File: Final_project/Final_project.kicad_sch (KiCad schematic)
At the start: 33 parts, among them U1 RP2040, U2 MCP1702T-3302E_CB, U3 ESP32-WROOM-32

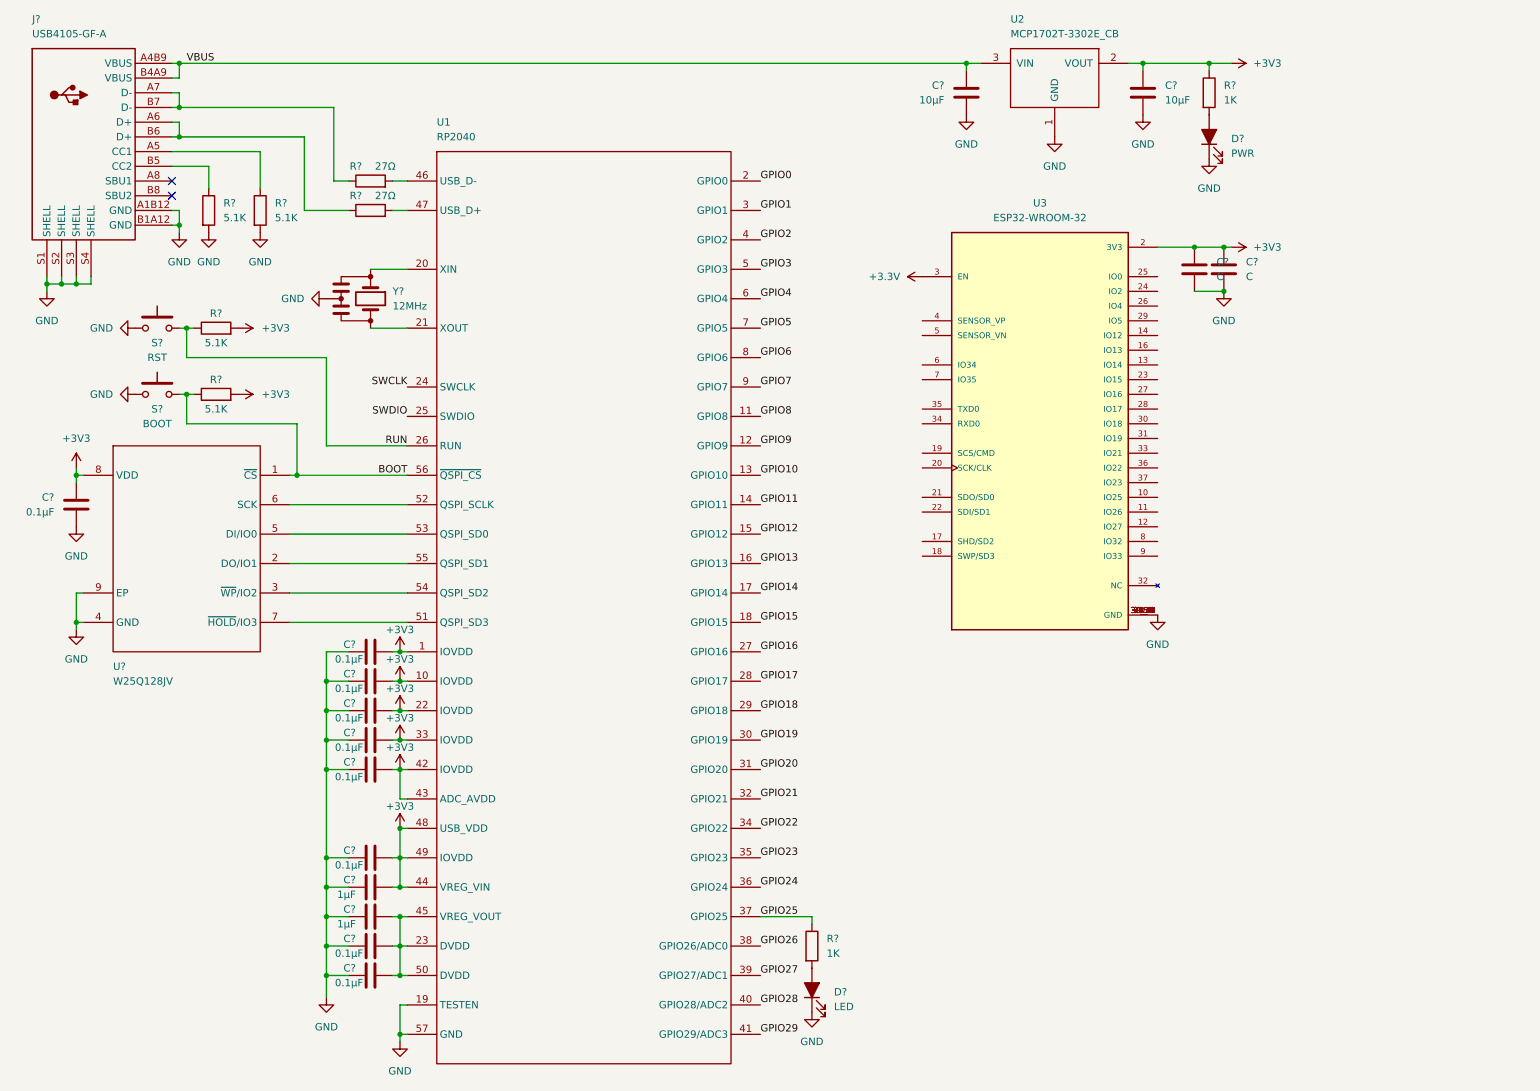
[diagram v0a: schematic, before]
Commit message: Add library and hierarchical schematic
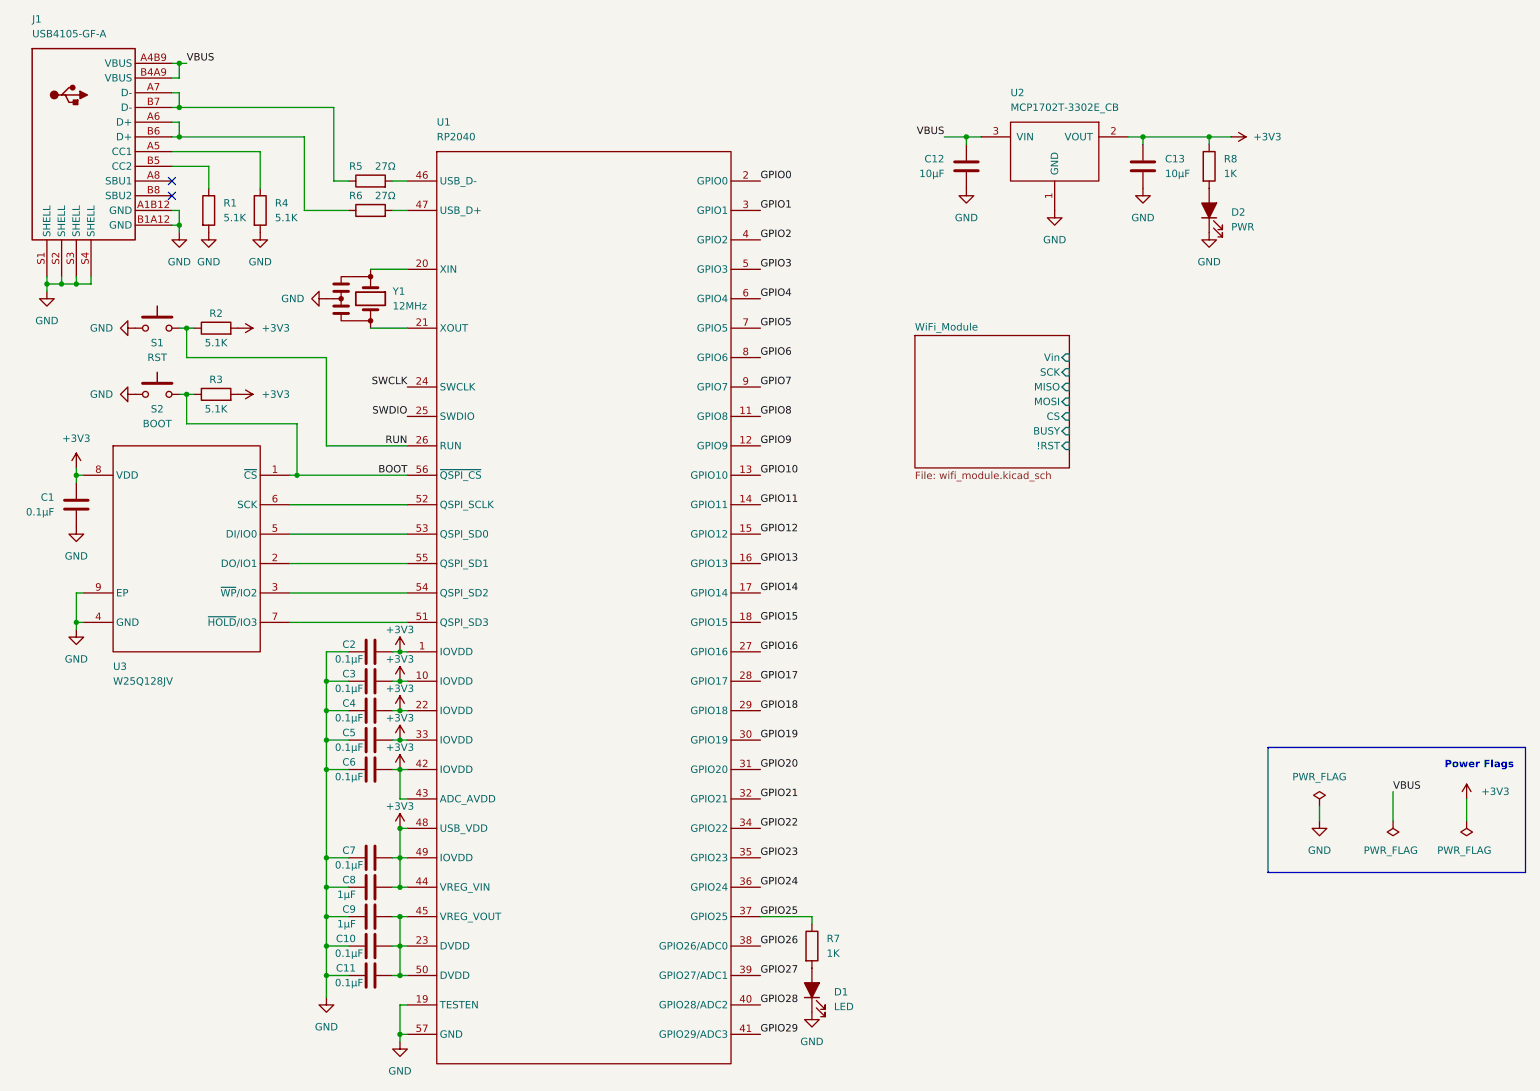
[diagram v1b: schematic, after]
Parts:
- removed C? (x2): C, symbol Device:C
- removed U3: ESP32-WROOM-32, MODULE_ESP32-WROOM-32, symbol ESP32-WROOM-32:ESP32-WROOM-32
- C1, C10, C11, C2, C3, C4, C5, C6, C7: renamed from C?; footprint Eclectronics_mp3:CL10B104JB8NNNC -> Final_project:CL10B104JB8NNNC
- C12, C13: renamed from C?; footprint Eclectronics_mp3:GRM188R61E106KA73D -> Final_project:GRM188R61E106KA73D
- C8, C9: renamed from C?; footprint Eclectronics_mp3:CL10B105KA8NNNC -> Final_project:CL10B105KA8NNNC
- D1: renamed from D?; footprint Eclectronics_mp3:LTST-C170TBKT -> Final_project:LTST-C170TBKT
- D2: renamed from D?; footprint Eclectronics_mp3:LTST-C170TGKT -> Final_project:LTST-C170TGKT
- J1: renamed from J?; footprint Eclectronics_mp3:USB4105-GF-A -> Final_project:USB4105-GF-A
- R1, R2, R3, R4: renamed from R?; footprint Eclectronics_mp3:RES_ERJ3EKF5101V -> Final_project:RES_ERJ3EKF5101V
- R5, R6, R7, R8: renamed from R?; footprint Eclectronics_mp3:RC0603FR-071KL -> Final_project:RC0603FR-071KL
- S1, S2: renamed from S?; footprint Eclectronics_mp3:KXT321LHS -> Final_project:KXT321LHS
- U1: footprint Eclectronics_mp3:RP2040 -> Final_project:RP2040
- U3: renamed from U?; footprint Eclectronics_mp3:MIC_WSON-8-M -> Final_project:MIC_WSON-8-M
- Y1: renamed from Y?; footprint Eclectronics_mp3:CSTNE -> Final_project:CSTNE
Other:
- added sheet WiFi_Module (wifi_module.kicad_sch)
- note added: "Power Flags"
- moved on the sheet: C12, C13, D2, R8, U2

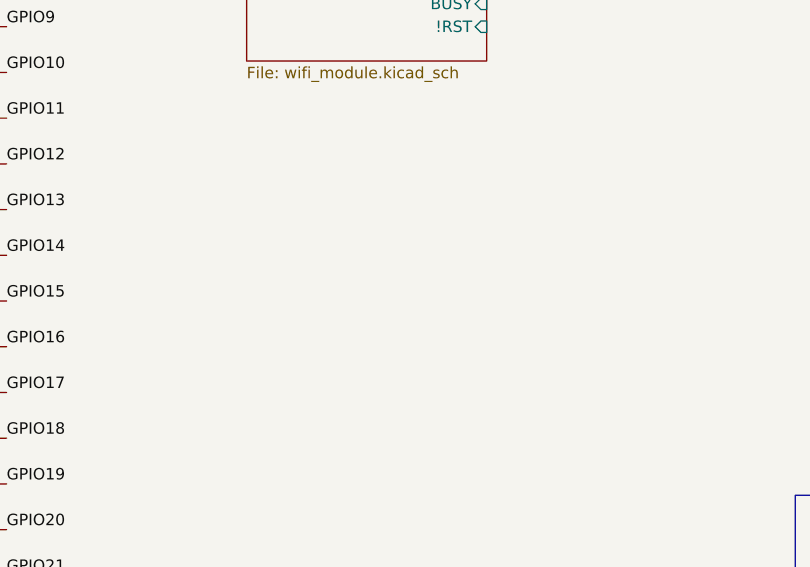
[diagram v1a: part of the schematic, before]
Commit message: added audiojack
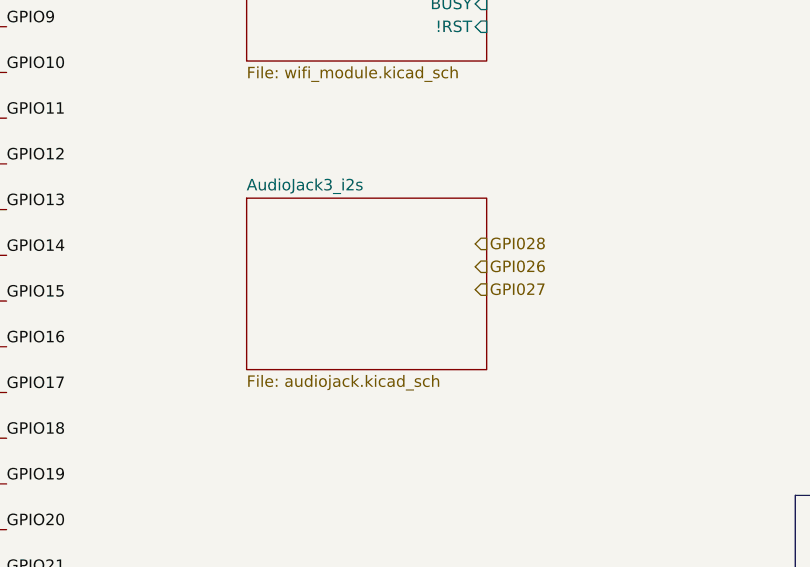
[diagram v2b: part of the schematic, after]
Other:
- added sheet AudioJack3_i2s (audiojack.kicad_sch)
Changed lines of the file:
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@@
     (effects (font (size 1.27 1.27)) (justify left bottom))
+  )
+  (hierarchical_label "GPI026" (shape input) (at 199.39 114.3 0)
+    (effects (font (size 1.27 1.27)) (justify left))
+  )
+  (hierarchical_label "GPI028" (shape input) (at 199.39 111.76 0)
+    (effects (font (size 1.27 1.27)) (justify left))
+  )
+  (hierarchical_label "GPI027" (shape input) (at 199.39 116.84 0)
+    (effects (font (size 1.27 1.27)) (justify left))
   )
   (symbol (lib_id "Device:C") (at 80.01 138.43 270) (unit 1)
@@
     )
   )
+  (sheet (at 173.99 106.68) (size 26.67 19.05) (fields_autoplaced)
+    (stroke (width 0.1524) (type solid) (color 0 0 0 0))
+    (fill (color 255 255 194 1.0000))
+    (property "Sheet name" "AudioJack3_i2s" (id 0) (at 173.99 105.9684 0)
+      (effects (font (size 1.27 1.27)) (justify left bottom))
+    )
+    (property "Sheet file" "audiojack.kicad_sch" (id 1) (at 173.99 126.3146 0)
+      (effects (font (size 1.27 1.27)) (justify left top))
+    )
+  )
   (sheet_instances
     (path "/" (page "1"))
     (path "/5f380518-a4aa-4cf5-aa47-79ba18474bc7" (page "2"))
+    (path "/a587f9f9-6d27-4989-a344-d47a4b55e4be" (page "3"))
   )
   (symbol_instances
@@
       (reference "#PWR0132") (unit 1) (value "GND") (footprint "")
     )
+    (path "/a587f9f9-6d27-4989-a344-d47a4b55e4be/0758e25a-39ba-4d34-abca-2bb40d5af830"
+      (reference "#PWR?") (unit 1) (value "GND") (footprint "")
+    )
+    (path "/a587f9f9-6d27-4989-a344-d47a4b55e4be/1b14fa98-daa4-474f-ab59-8b8ff9ad2252"
+      (reference "#PWR?") (unit 1) (value "GND") (footprint "")
+    )
+    (path "/a587f9f9-6d27-4989-a344-d47a4b55e4be/4261c671-797a-4dce-b779-2a1cca3a497a"
+      (reference "#PWR?") (unit 1) (value "GND") (footprint "")
+    )
+    (path "/a587f9f9-6d27-4989-a344-d47a4b55e4be/49961937-da64-4a79-b32e-b550e5b13812"
+      (reference "#PWR?") (unit 1) (value "GND") (footprint "")
+    )
+    (path "/a587f9f9-6d27-4989-a344-d47a4b55e4be/4a0c82ab-f8f8-4889-9bab-585f3ddf17f0"
+      (reference "#PWR?") (unit 1) (value "GND") (footprint "")
+    )
+    (path "/a587f9f9-6d27-4989-a344-d47a4b55e4be/60d3bdc0-5ca1-4a26-b977-3b85a79f9bd8"
+      (reference "#PWR?") (unit 1) (value "GND") (footprint "")
+    )
+    (path "/a587f9f9-6d27-4989-a344-d47a4b55e4be/6768cd5a-a081-418d-bb8c-15ae6a2958b1"
+      (reference "#PWR?") (unit 1) (value "GND") (footprint "")
+    )
+    (path "/a587f9f9-6d27-4989-a344-d47a4b55e4be/6a4163df-9085-4be2-840b-f3d0d2548868"
+      (reference "#PWR?") (unit 1) (value "+3.3V") (footprint "")
+    )
+    (path "/a587f9f9-6d27-4989-a344-d47a4b55e4be/74c14a05-ea6b-4019-8abd-25eb1a6fc3bc"
+      (reference "#PWR?") (unit 1) (value "GND") (footprint "")
+    )
+    (path "/a587f9f9-6d27-4989-a344-d47a4b55e4be/8d23dbde-8b01-4c96-b6b9-2cd0d701c902"
+      (reference "#PWR?") (unit 1) (value "+3.3VA") (footprint "")
+    )
+    (path "/a587f9f9-6d27-4989-a344-d47a4b55e4be/941fd3b4-a86c-4982-94f3-d22033298fcf"
+      (reference "#PWR?") (unit 1) (value "GND") (footprint "")
+    )
+    (path "/a587f9f9-6d27-4989-a344-d47a4b55e4be/d754a0cf-27fb-43d7-96e5-e22e0806c88b"
+      (reference "#PWR?") (unit 1) (value "+3.3V") (footprint "")
+    )
+    (path "/a587f9f9-6d27-4989-a344-d47a4b55e4be/fdd1049d-4353-4894-a8db-3df85b208654"
+      (reference "#PWR?") (unit 1) (value "GND") (footprint "")
+    )
     (path "/4185e825-d3db-49f7-84c3-1d674f768766"
       (reference "C1") (unit 1) (value "0.1µF") (footprint "Final_project:CL10B104JB8NNNC")
@@
       (reference "C15") (unit 1) (value "C") (footprint "Capacitor_SMD:C_0603_1608Metric")
     )
+    (path "/a587f9f9-6d27-4989-a344-d47a4b55e4be/108086f3-c1df-4566-84bd-fbc60614202b"
+      (reference "C?") (unit 1) (value "10u") (footprint "Capacitor_SMD:C_0603_1608Metric")
+    )
+    (path "/a587f9f9-6d27-4989-a344-d47a4b55e4be/32442a1c-8e05-4bad-b894-204e8dac19bb"
+      (reference "C?") (unit 1) (value "2.2n") (footprint "Capacitor_SMD:C_0402_1005Metric")
+    )
+    (path "/a587f9f9-6d27-4989-a344-d47a4b55e4be/4c6a2e57-abe7-478c-a1a6-024cf77305b0"
+      (reference "C?") (unit 1) (value "100n") (footprint "Capacitor_SMD:C_0402_1005Metric")
+    )
+    (path "/a587f9f9-6d27-4989-a344-d47a4b55e4be/6ca33c87-f79e-4a26-9f94-3927f1b5c179"
+      (reference "C?") (unit 1) (value "2.2u") (footprint "Capacitor_SMD:C_0603_1608Metric")
+    )
+    (path "/a587f9f9-6d27-4989-a344-d47a4b55e4be/70985074-b4dd-4282-bf81-f45bdab6ee8e"
+      (reference "C?") (unit 1) (value "10u") (footprint "Capacitor_SMD:C_0603_1608Metric")
+    )
+    (path "/a587f9f9-6d27-4989-a344-d47a4b55e4be/825af33a-d88e-4844-a2b2-fcc455893256"
+      (reference "C?") (unit 1) (value "100n") (footprint "Capacitor_SMD:C_0402_1005Metric")
+    )
+    (path "/a587f9f9-6d27-4989-a344-d47a4b55e4be/a8ef7a4d-08e8-40a1-96aa-2409cbe8b2f4"
+      (reference "C?") (unit 1) (value "2.2u") (footprint "Capacitor_SMD:C_0603_1608Metric")
+    )
+    (path "/a587f9f9-6d27-4989-a344-d47a4b55e4be/b2ae8a85-0718-4b79-bbda-e04acbe0ead8"
+      (reference "C?") (unit 1) (value "100n") (footprint "Capacitor_SMD:C_0402_1005Metric")
+    )
+    (path "/a587f9f9-6d27-4989-a344-d47a4b55e4be/b6bd64e6-b71d-475f-8470-2eb9494b5085"
+      (reference "C?") (unit 1) (value "2.2n") (footprint "Capacitor_SMD:C_0402_1005Metric")
+    )
+    (path "/a587f9f9-6d27-4989-a344-d47a4b55e4be/e7da94f5-848e-40b4-8637-cf00b00efb40"
+      (reference "C?") (unit 1) (value "100n") (footprint "Capacitor_SMD:C_0402_1005Metric")
+    )
+    (path "/a587f9f9-6d27-4989-a344-d47a4b55e4be/f55247b4-ee21-4d4a-a61b-bed01368ee29"
+      (reference "C?") (unit 1) (value "10u") (footprint "Capacitor_SMD:C_0603_1608Metric")
+    )
     (path "/c2461336-3de5-4651-bacc-5ee03cccd9eb"
       (reference "D1") (unit 1) (value "LED") (footprint "Final_project:LTST-C170TBKT")
@@
       (reference "J1") (unit 1) (value "USB4105-GF-A") (footprint "Final_project:USB4105-GF-A")
     )
+    (path "/a587f9f9-6d27-4989-a344-d47a4b55e4be/c28a5e24-221c-40fa-8ba9-afc4f06db76b"
+      (reference "J?") (unit 1) (value "AudioJack3") (footprint "")
+    )
     (path "/6e52ec09-aa2b-4fd4-928b-f8255f408a1b"
       (reference "R1") (unit 1) (value "5.1K") (footprint "Final_project:RES_ERJ3EKF5101V")
@@
       (reference "R8") (unit 1) (value "1K") (footprint "Final_project:RC0603FR-071KL")
     )
+    (path "/a587f9f9-6d27-4989-a344-d47a4b55e4be/1505f0e3-c2eb-4222-a4a1-e5685bd3303c"
+      (reference "R?") (unit 1) (value "470") (footprint "Resistor_SMD:R_0402_1005Metric")
+    )
+    (path "/a587f9f9-6d27-4989-a344-d47a4b55e4be/c6995ec6-c0f5-459e-89ca-a639d2e964fe"
+      (reference "R?") (unit 1) (value "470") (footprint "Resistor_SMD:R_0402_1005Metric")
+    )
     (path "/d88ecd80-f389-40aa-8f67-79097bb2830a"
       (reference "S1") (unit 1) (value "RST") (footprint "Final_project:KXT321LHS")
@@
       (reference "U4") (unit 1) (value "ESP32-WROOM-32") (footprint "Final_project:MODULE_ESP32-WROOM-32")
     )
+    (path "/a587f9f9-6d27-4989-a344-d47a4b55e4be/d67d2ef1-789c-4fc0-8ba4-e2f7056af080"
+      (reference "U?") (unit 1) (value "PCM5101A") (footprint "Package_SO:TSSOP-20_4.4x6.5mm_P0.65mm")
+    )
     (path "/b995bef3-23bd-41bd-824d-90a30eae13e1"
